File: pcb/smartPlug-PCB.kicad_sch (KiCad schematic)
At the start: 10 parts, among them J1 Screw_Terminal_01x02, J2 Screw_Terminal_01x02, K1 SRD-05VDC-SL-C, Q1 2N3904, SW2 SW_Push, U1 ESP32-C3_SUPERMINI_TH, U2 HLK-PM01

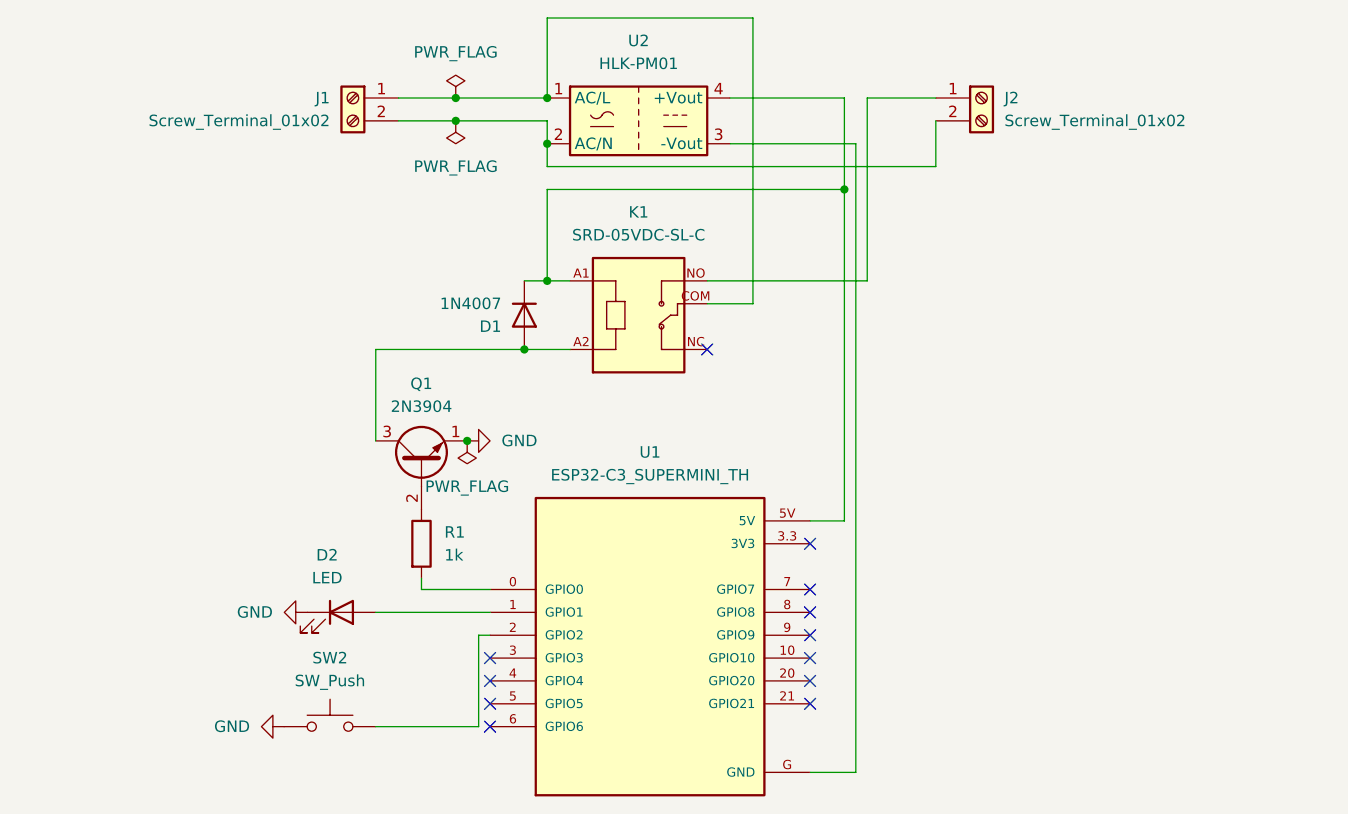
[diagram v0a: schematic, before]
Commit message: Added relay toggling, tested. Added a missing ground trace to PCB, regenereated gerbers.
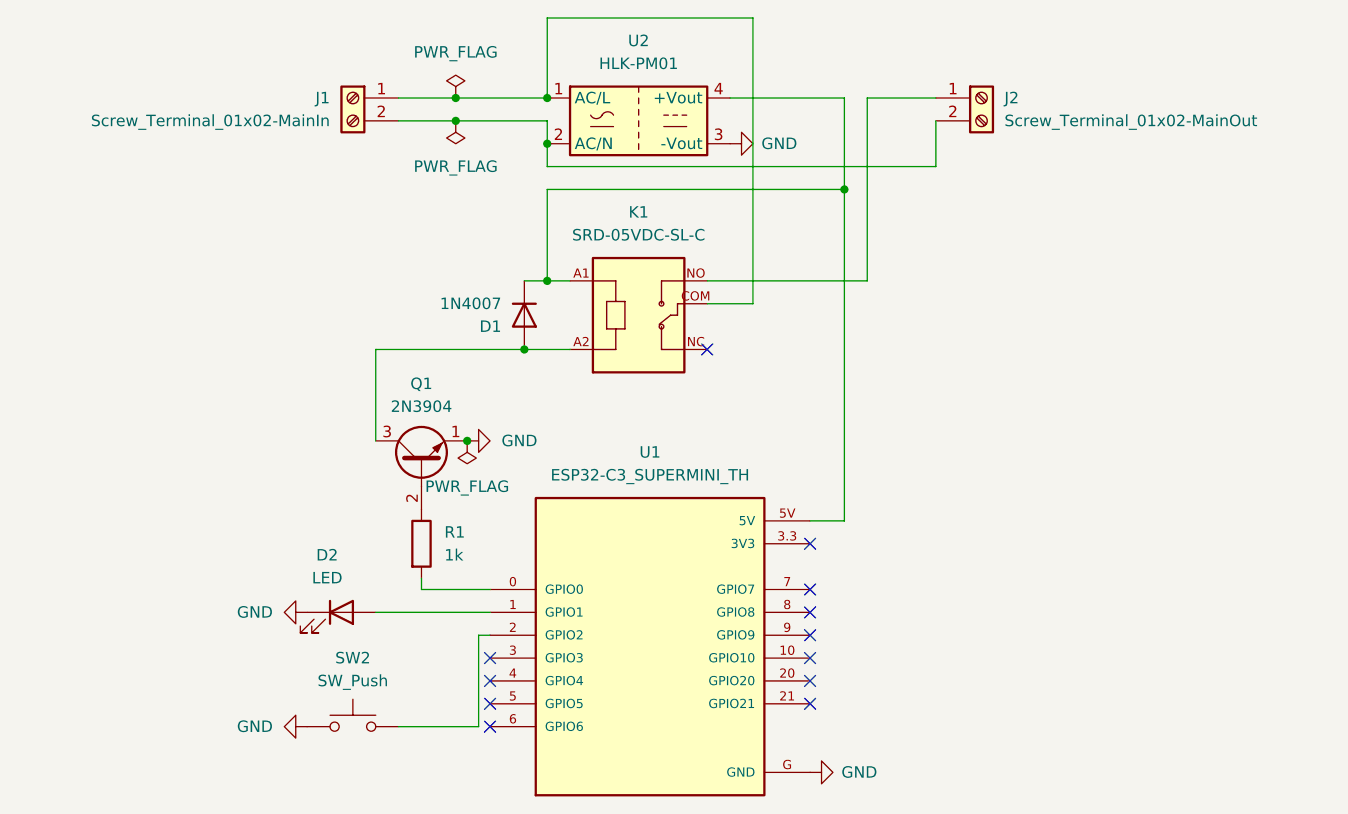
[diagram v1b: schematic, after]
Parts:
- J1: value Screw_Terminal_01x02 -> Screw_Terminal_01x02-MainIn
- J2: value Screw_Terminal_01x02 -> Screw_Terminal_01x02-MainOut
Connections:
- net GND: now also U1.G (GND), U2.3 (-Vout)
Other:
- moved on the sheet: SW2
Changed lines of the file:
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@@
 	(wire
 		(pts
-			(xy 128.27 130.81) (xy 116.84 130.81)
+			(xy 128.27 130.81) (xy 119.38 130.81)
 		)
 		(stroke
@@
 	(wire
 		(pts
-			(xy 170.18 135.89) (xy 165.1 135.89)
-		)
-		(stroke
-			(width 0)
-			(type default)
-		)
-	)
-	(wire
-		(pts
 			(xy 168.91 71.12) (xy 168.91 107.95)
 		)
@@
 	(wire
 		(pts
-			(xy 170.18 66.04) (xy 170.18 135.89)
-		)
-		(stroke
-			(width 0)
-			(type default)
-		)
-	)
-	(wire
-		(pts
 			(xy 133.35 81.28) (xy 135.89 81.28)
 		)
@@
 		(pts
 			(xy 171.45 60.96) (xy 179.07 60.96)
-		)
-		(stroke
-			(width 0)
-			(type default)
-		)
-	)
-	(wire
-		(pts
-			(xy 156.21 66.04) (xy 170.18 66.04)
 		)
 		(stroke
@@
 	)
 	(symbol
+		(lib_id "power:GND")
+		(at 165.1 135.89 90)
+		(unit 1)
+		(body_style 1)
+		(exclude_from_sim no)
+		(in_bom yes)
+		(on_board yes)
+		(in_pos_files yes)
+		(dnp no)
+		(fields_autoplaced yes)
+		(property "Reference" "#PWR04"
+			(at 171.45 135.89 0)
+			(hide yes)
+			(show_name no)
+			(do_not_autoplace no)
+			(effects
+				(font
+					(size 1.27 1.27)
+				)
+			)
+		)
+		(property "Value" "GND"
+			(at 168.5762 135.8899 90)
+			(show_name no)
+			(do_not_autoplace no)
+			(effects
+				(font
+					(size 1.27 1.27)
+				)
+				(justify right)
+			)
+		)
+		(property "Footprint" ""
+			(at 165.1 135.89 0)
+			(hide yes)
+			(show_name no)
+			(do_not_autoplace no)
+			(effects
+				(font
+					(size 1.27 1.27)
+				)
+			)
+		)
+		(property "Datasheet" ""
+			(at 165.1 135.89 0)
+			(hide yes)
+			(show_name no)
+			(do_not_autoplace no)
+			(effects
+				(font
+					(size 1.27 1.27)
+				)
+			)
+		)
+		(property "Description" "Power symbol creates a global label with name \"GND\" , ground"
+			(at 165.1 135.89 0)
+			(hide yes)
+			(show_name no)
+			(do_not_autoplace no)
+			(effects
+				(font
+					(size 1.27 1.27)
+				)
+			)
+		)
+		(pin "1"
+		)
+		(instances
+			(project "smartPlug-PCB"
+				(path "/807b7313-a2e5-4ef1-ac87-c4d49ba477c3"
+					(reference "#PWR04")
+					(unit 1)
+				)
+			)
+		)
+	)
+	(symbol
 		(lib_id "Converter_ACDC:HLK-PM01")
 		(at 146.05 63.5 0)
@@
 	(symbol
 		(lib_id "Switch:SW_Push")
-		(at 111.76 130.81 0)
+		(at 114.3 130.81 0)
 		(unit 1)
 		(body_style 1)
@@
 		(fields_autoplaced yes)
 		(property "Reference" "SW2"
-			(at 111.76 123.19 0)
+			(at 114.3 123.19 0)
 			(show_name no)
 			(do_not_autoplace no)
@@
 		)
 		(property "Value" "SW_Push"
-			(at 111.76 125.73 0)
+			(at 114.3 125.73 0)
 			(show_name no)
 			(do_not_autoplace no)
@@
 		)
 		(property "Footprint" "Button_Switch_THT:SW_PUSH_6mm"
-			(at 111.76 125.73 0)
+			(at 114.3 125.73 0)
 			(hide yes)
 			(show_name no)
@@
 		)
 		(property "Datasheet" ""
-			(at 111.76 125.73 0)
+			(at 114.3 125.73 0)
 			(hide yes)
 			(show_name no)
@@
 		)
 		(property "Description" "Push button switch, generic, two pins"
-			(at 111.76 130.81 0)
+			(at 114.3 130.81 0)
 			(hide yes)
 			(show_name no)
@@
 			)
 		)
-		(property "Value" "Screw_Terminal_01x02"
+		(property "Value" "Screw_Terminal_01x02-MainOut"
 			(at 186.69 63.4999 0)
 			(show_name no)
@@
 	)
 	(symbol
+		(lib_id "power:GND")
+		(at 156.21 66.04 90)
+		(unit 1)
+		(body_style 1)
+		(exclude_from_sim no)
+		(in_bom yes)
+		(on_board yes)
+		(in_pos_files yes)
+		(dnp no)
+		(fields_autoplaced yes)
+		(property "Reference" "#PWR05"
+			(at 162.56 66.04 0)
+			(hide yes)
+			(show_name no)
+			(do_not_autoplace no)
+			(effects
+				(font
+					(size 1.27 1.27)
+				)
+			)
+		)
+		(property "Value" "GND"
+			(at 159.6862 66.0399 90)
+			(show_name no)
+			(do_not_autoplace no)
+			(effects
+				(font
+					(size 1.27 1.27)
+				)
+				(justify right)
+			)
+		)
+		(property "Footprint" ""
+			(at 156.21 66.04 0)
+			(hide yes)
+			(show_name no)
+			(do_not_autoplace no)
+			(effects
+				(font
+					(size 1.27 1.27)
+				)
+			)
+		)
+		(property "Datasheet" ""
+			(at 156.21 66.04 0)
+			(hide yes)
+			(show_name no)
+			(do_not_autoplace no)
+			(effects
+				(font
+					(size 1.27 1.27)
+				)
+			)
+		)
+		(property "Description" "Power symbol creates a global label with name \"GND\" , ground"
+			(at 156.21 66.04 0)
+			(hide yes)
+			(show_name no)
+			(do_not_autoplace no)
+			(effects
+				(font
+					(size 1.27 1.27)
+				)
+			)
+		)
+		(pin "1"
+		)
+		(instances
+			(project "smartPlug-PCB"
+				(path "/807b7313-a2e5-4ef1-ac87-c4d49ba477c3"
+					(reference "#PWR05")
+					(unit 1)
+				)
+			)
+		)
+	)
+	(symbol
 		(lib_id "Diode:1N4007")
 		(at 133.35 85.09 270)
@@
 	(symbol
 		(lib_id "power:GND")
-		(at 106.68 130.81 270)
+		(at 109.22 130.81 270)
 		(unit 1)
 		(body_style 1)
@@
 		(fields_autoplaced yes)
 		(property "Reference" "#PWR03"
-			(at 100.33 130.81 0)
+			(at 102.87 130.81 0)
 			(hide yes)
 			(show_name no)
@@
 		)
 		(property "Value" "GND"
-			(at 102.87 130.8099 90)
+			(at 105.41 130.8099 90)
 			(show_name no)
 			(do_not_autoplace no)
@@
 		)
 		(property "Footprint" ""
-			(at 106.68 130.81 0)
+			(at 109.22 130.81 0)
 			(hide yes)
 			(show_name no)
@@
 		)
 		(property "Datasheet" ""
-			(at 106.68 130.81 0)
+			(at 109.22 130.81 0)
 			(hide yes)
 			(show_name no)
@@
 		)
 		(property "Description" "Power symbol creates a global label with name \"GND\" , ground"
-			(at 106.68 130.81 0)
+			(at 109.22 130.81 0)
 			(hide yes)
 			(show_name no)
@@
 			)
 		)
-		(property "Value" "Screw_Terminal_01x02"
+		(property "Value" "Screw_Terminal_01x02-MainIn"
 			(at 111.76 63.4999 0)
 			(show_name no)

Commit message: Respun PCB. Replaced LED with onboard LED in FW.
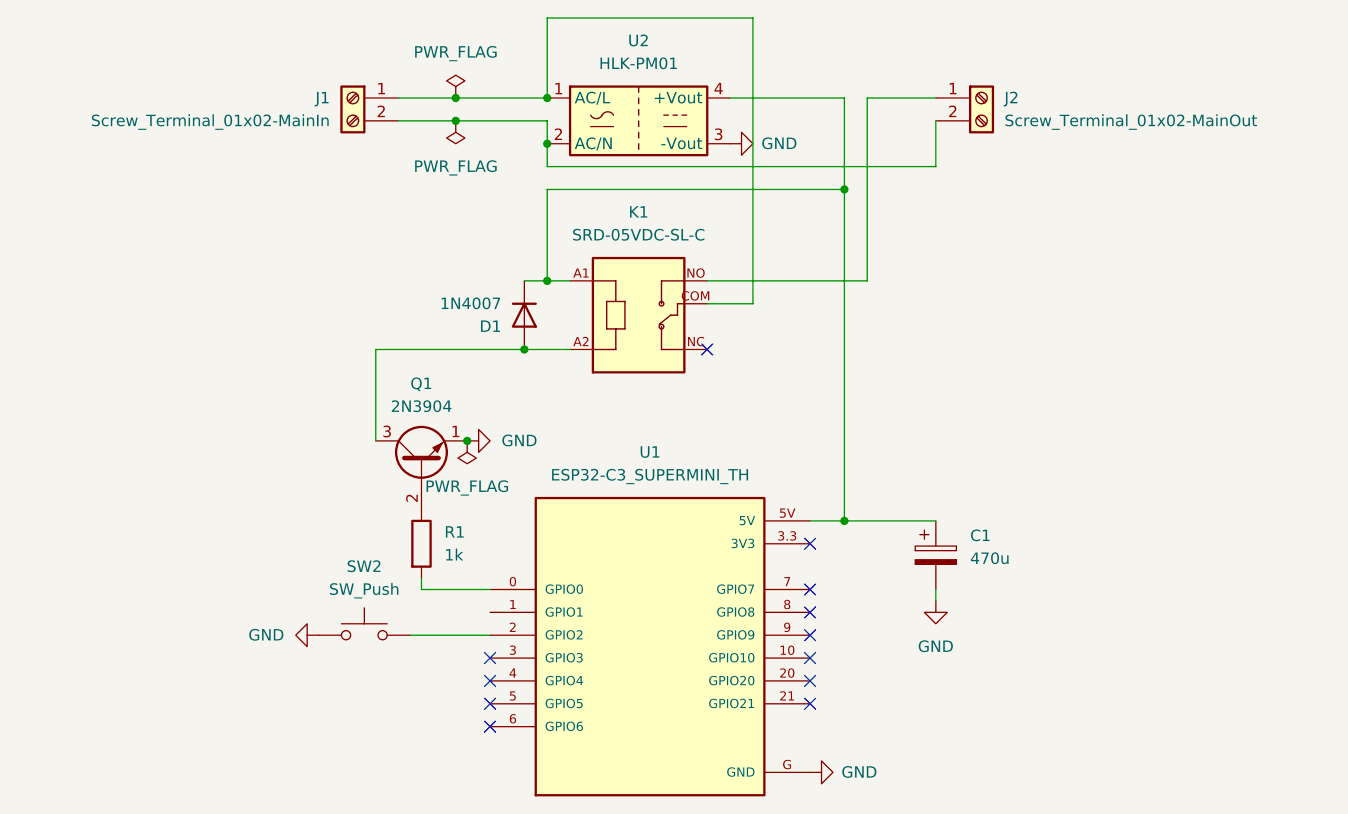
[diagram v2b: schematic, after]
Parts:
- removed D2: LED, LED_THT:LED_D5.0mm, symbol Device:LED
- added C1: 470u, Capacitor_THT:CP_Radial_D8.0mm_P3.50mm, symbol Device:C_Polarized
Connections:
- net GND: now also C1.2
- net at D1.1 (K), K1.A1, U1.5V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: now also C1.1
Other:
- moved on the sheet: SW2
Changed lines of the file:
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@@
+	)
+	(junction
+		(at 168.91 107.95)
+		(diameter 0)
+		(color 0 0 0 0)
 	)
 	(junction
@@
 	(wire
 		(pts
-			(xy 128.27 130.81) (xy 119.38 130.81)
+			(xy 120.65 120.65) (xy 129.54 120.65)
 		)
 		(stroke
@@
 	(wire
 		(pts
-			(xy 116.84 118.11) (xy 129.54 118.11)
-		)
-		(stroke
-			(width 0)
-			(type default)
-		)
-	)
-	(wire
-		(pts
 			(xy 158.75 52.07) (xy 135.89 52.07)
 		)
@@
 	(wire
 		(pts
-			(xy 128.27 120.65) (xy 128.27 130.81)
-		)
-		(stroke
-			(width 0)
-			(type default)
-		)
-	)
-	(wire
-		(pts
 			(xy 135.89 63.5) (xy 135.89 66.04)
 		)
@@
 	(wire
 		(pts
+			(xy 179.07 107.95) (xy 168.91 107.95)
+		)
+		(stroke
+			(width 0)
+			(type default)
+		)
+	)
+	(wire
+		(pts
 			(xy 168.91 71.12) (xy 168.91 107.95)
 		)
@@
 	(wire
 		(pts
-			(xy 129.54 120.65) (xy 128.27 120.65)
+			(xy 179.07 115.57) (xy 179.07 116.84)
 		)
 		(stroke
@@
 	(symbol
 		(lib_id "power:GND")
-		(at 109.22 118.11 270)
-		(unit 1)
-		(body_style 1)
-		(exclude_from_sim no)
-		(in_bom yes)
-		(on_board yes)
-		(in_pos_files yes)
-		(dnp no)
-		(fields_autoplaced yes)
-		(property "Reference" "#PWR02"
-			(at 102.87 118.11 0)
-			(hide yes)
-			(show_name no)
-			(do_not_autoplace no)
-			(effects
-				(font
-					(size 1.27 1.27)
-				)
-			)
-		)
-		(property "Value" "GND"
-			(at 105.41 118.1099 90)
-			(show_name no)
-			(do_not_autoplace no)
-			(effects
-				(font
-					(size 1.27 1.27)
-				)
-				(justify right)
-			)
-		)
-		(property "Footprint" ""
-			(at 109.22 118.11 0)
-			(hide yes)
-			(show_name no)
-			(do_not_autoplace no)
-			(effects
-				(font
-					(size 1.27 1.27)
-				)
-			)
-		)
-		(property "Datasheet" ""
-			(at 109.22 118.11 0)
-			(hide yes)
-			(show_name no)
-			(do_not_autoplace no)
-			(effects
-				(font
-					(size 1.27 1.27)
-				)
-			)
-		)
-		(property "Description" "Power symbol creates a global label with name \"GND\" , ground"
-			(at 109.22 118.11 0)
-			(hide yes)
-			(show_name no)
-			(do_not_autoplace no)
-			(effects
-				(font
-					(size 1.27 1.27)
-				)
-			)
-		)
-		(pin "1"
-		)
-		(instances
-			(project "smartPlug-PCB"
-				(path "/807b7313-a2e5-4ef1-ac87-c4d49ba477c3"
-					(reference "#PWR02")
-					(unit 1)
-				)
-			)
-		)
-	)
-	(symbol
-		(lib_id "power:GND")
 		(at 127 99.06 90)
 		(unit 1)
@@
 	(symbol
 		(lib_id "Switch:SW_Push")
-		(at 114.3 130.81 0)
+		(at 115.57 120.65 0)
 		(unit 1)
 		(body_style 1)
@@
 		(fields_autoplaced yes)
 		(property "Reference" "SW2"
-			(at 114.3 123.19 0)
+			(at 115.57 113.03 0)
 			(show_name no)
 			(do_not_autoplace no)
@@
 		)
 		(property "Value" "SW_Push"
-			(at 114.3 125.73 0)
+			(at 115.57 115.57 0)
 			(show_name no)
 			(do_not_autoplace no)
@@
 		)
 		(property "Footprint" "Button_Switch_THT:SW_PUSH_6mm"
-			(at 114.3 125.73 0)
+			(at 115.57 115.57 0)
 			(hide yes)
 			(show_name no)
@@
 		)
 		(property "Datasheet" ""
-			(at 114.3 125.73 0)
+			(at 115.57 115.57 0)
 			(hide yes)
 			(show_name no)
@@
 		)
 		(property "Description" "Push button switch, generic, two pins"
-			(at 114.3 130.81 0)
+			(at 115.57 120.65 0)
 			(hide yes)
 			(show_name no)
@@
 	)
 	(symbol
+		(lib_id "Device:C_Polarized")
+		(at 179.07 111.76 0)
+		(unit 1)
+		(body_style 1)
+		(exclude_from_sim no)
+		(in_bom yes)
+		(on_board yes)
+		(in_pos_files yes)
+		(dnp no)
+		(fields_autoplaced yes)
+		(property "Reference" "C1"
+			(at 182.88 109.6009 0)
+			(show_name no)
+			(do_not_autoplace no)
+			(effects
+				(font
+					(size 1.27 1.27)
+				)
+				(justify left)
+			)
+		)
+		(property "Value" "470u"
+			(at 182.88 112.1409 0)
+			(show_name no)
+			(do_not_autoplace no)
+			(effects
+				(font
+					(size 1.27 1.27)
+				)
+				(justify left)
+			)
+		)
+		(property "Footprint" "Capacitor_THT:CP_Radial_D8.0mm_P3.50mm"
+			(at 180.0352 115.57 0)
+			(hide yes)
+			(show_name no)
+			(do_not_autoplace no)
+			(effects
+				(font
+					(size 1.27 1.27)
+				)
+			)
+		)
+		(property "Datasheet" ""
+			(at 179.07 111.76 0)
+			(hide yes)
+			(show_name no)
+			(do_not_autoplace no)
+			(effects
+				(font
+					(size 1.27 1.27)
+				)
+			)
+		)
+		(property "Description" "Polarized capacitor"
+			(at 179.07 111.76 0)
+			(hide yes)
+			(show_name no)
+			(do_not_autoplace no)
+			(effects
+				(font
+					(size 1.27 1.27)
+				)
+			)
+		)
+		(pin "2"
+		)
+		(pin "1"
+		)
+		(instances
+			(project "smartPlug-PCB"
+				(path "/807b7313-a2e5-4ef1-ac87-c4d49ba477c3"
+					(reference "C1")
+					(unit 1)
+				)
+			)
+		)
+	)
+	(symbol
 		(lib_id "power:GND")
-		(at 109.22 130.81 270)
+		(at 110.49 120.65 270)
 		(unit 1)
 		(body_style 1)
@@
 		(fields_autoplaced yes)
 		(property "Reference" "#PWR03"
-			(at 102.87 130.81 0)
+			(at 104.14 120.65 0)
 			(hide yes)
 			(show_name no)
@@
 		)
 		(property "Value" "GND"
-			(at 105.41 130.8099 90)
+			(at 106.68 120.6499 90)
 			(show_name no)
 			(do_not_autoplace no)
@@
 		)
 		(property "Footprint" ""
-			(at 109.22 130.81 0)
+			(at 110.49 120.65 0)
 			(hide yes)
 			(show_name no)
@@
 		)
 		(property "Datasheet" ""
-			(at 109.22 130.81 0)
+			(at 110.49 120.65 0)
 			(hide yes)
 			(show_name no)
@@
 		)
 		(property "Description" "Power symbol creates a global label with name \"GND\" , ground"
-			(at 109.22 130.81 0)
+			(at 110.49 120.65 0)
 			(hide yes)
 			(show_name no)
@@
 	)
 	(symbol
-		(lib_id "Device:LED")
-		(at 113.03 118.11 0)
+		(lib_id "power:GND")
+		(at 179.07 116.84 0)
 		(unit 1)
 		(body_style 1)
@@
 		(dnp no)
 		(fields_autoplaced yes)
-		(property "Reference" "D2"
-			(at 111.4425 111.76 0)
-			(show_name no)
-			(do_not_autoplace no)
-			(effects
-				(font
-					(size 1.27 1.27)
-				)
-			)
-		)
-		(property "Value" "LED"
-			(at 111.4425 114.3 0)
-			(show_name no)
-			(do_not_autoplace no)
-			(effects
-				(font
-					(size 1.27 1.27)
-				)
-			)
-		)
-		(property "Footprint" "LED_THT:LED_D5.0mm"
-			(at 113.03 118.11 0)
+		(property "Reference" "#PWR06"
+			(at 179.07 123.19 0)
+			(hide yes)
+			(show_name no)
+			(do_not_autoplace no)
+			(effects
+				(font
+					(size 1.27 1.27)
+				)
+			)
+		)
+		(property "Value" "GND"
+			(at 179.07 121.92 0)
+			(show_name no)
+			(do_not_autoplace no)
+			(effects
+				(font
+					(size 1.27 1.27)
+				)
+			)
+		)
+		(property "Footprint" ""
+			(at 179.07 116.84 0)
 			(hide yes)
 			(show_name no)
@@
 		)
 		(property "Datasheet" ""
-			(at 113.03 118.11 0)
-			(hide yes)
-			(show_name no)
-			(do_not_autoplace no)
-			(effects
-				(font
-					(size 1.27 1.27)
-				)
-			)
-		)
-		(property "Description" "Light emitting diode"
-			(at 113.03 118.11 0)
-			(hide yes)
-			(show_name no)
-			(do_not_autoplace no)
-			(effects
-				(font
-					(size 1.27 1.27)
-				)
-			)
-		)
-		(property "Sim.Pins" "1=K 2=A"
-			(at 113.03 118.11 0)
-			(hide yes)
-			(show_name no)
-			(do_not_autoplace no)
-			(effects
-				(font
-					(size 1.27 1.27)
-				)
-			)
-		)
-		(pin "2"
+			(at 179.07 116.84 0)
+			(hide yes)
+			(show_name no)
+			(do_not_autoplace no)
+			(effects
+				(font
+					(size 1.27 1.27)
+				)
+			)
+		)
+		(property "Description" "Power symbol creates a global label with name \"GND\" , ground"
+			(at 179.07 116.84 0)
+			(hide yes)
+			(show_name no)
+			(do_not_autoplace no)
+			(effects
+				(font
+					(size 1.27 1.27)
+				)
+			)
 		)
 		(pin "1"
@@
 			(project "smartPlug-PCB"
 				(path "/807b7313-a2e5-4ef1-ac87-c4d49ba477c3"
-					(reference "D2")
+					(reference "#PWR06")
 					(unit 1)
 				)
